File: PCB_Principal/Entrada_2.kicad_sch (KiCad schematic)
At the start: 17 parts, among them U41 TL071

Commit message: Iniciando PCB...
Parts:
- U151: renamed from U41; footprint Package_DIP:CERDIP-8_W7.62mm_SideBrazed_LongPads_Socket -> Package_DIP:CERDIP-8_W7.62mm_SideBrazed_LongPads
- renumbered C41 to C151, C42 to C152, C43 to C153, C44 to C154, C45 to C155, D41 to D151, D42 to D152, R41 to R151, R42 to R152, R43 to R153, R44 to R154, R45 to R155, R46 to R156, R47 to R157, R48 to R158, RV41 to RV151
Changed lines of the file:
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@@
 		(on_board yes)
 		(dnp no)
-		(property "Reference" "R44"
+		(property "Reference" "R154"
 			(at 185.42 91.948 90)
 			(effects
@@
 			(project "ISPEL-CAD_v1"
 				(path "/f66f0001-c0b9-4d2c-a26f-f2bac9dfd594/18a53c06-5390-4a02-a62f-2bcfe4b4c6e4"
-					(reference "R44")
+					(reference "R154")
 					(unit 1)
 				)
@@
 		(on_board yes)
 		(dnp no)
-		(property "Reference" "R42"
+		(property "Reference" "R152"
 			(at 104.14 89.408 90)
 			(effects
@@
 			(project "ISPEL-CAD_v1"
 				(path "/f66f0001-c0b9-4d2c-a26f-f2bac9dfd594/18a53c06-5390-4a02-a62f-2bcfe4b4c6e4"
-					(reference "R42")
+					(reference "R152")
 					(unit 1)
 				)
@@
 		(on_board yes)
 		(dnp no)
-		(property "Reference" "R47"
+		(property "Reference" "R157"
 			(at 209.55 86.36 0)
 			(effects
@@
 			(project "ISPEL-CAD_v1"
 				(path "/f66f0001-c0b9-4d2c-a26f-f2bac9dfd594/18a53c06-5390-4a02-a62f-2bcfe4b4c6e4"
-					(reference "R47")
+					(reference "R157")
 					(unit 1)
 				)
@@
 		(on_board yes)
 		(dnp no)
-		(property "Reference" "R46"
+		(property "Reference" "R156"
 			(at 201.93 91.948 90)
 			(effects
@@
 			(project "ISPEL-CAD_v1"
 				(path "/f66f0001-c0b9-4d2c-a26f-f2bac9dfd594/18a53c06-5390-4a02-a62f-2bcfe4b4c6e4"
-					(reference "R46")
+					(reference "R156")
 					(unit 1)
 				)
@@
 		(on_board yes)
 		(dnp no)
-		(property "Reference" "R43"
+		(property "Reference" "R153"
 			(at 111.76 99.06 0)
 			(effects
@@
 			(project "ISPEL-CAD_v1"
 				(path "/f66f0001-c0b9-4d2c-a26f-f2bac9dfd594/18a53c06-5390-4a02-a62f-2bcfe4b4c6e4"
-					(reference "R43")
+					(reference "R153")
 					(unit 1)
 				)
@@
 		(dnp no)
 		(fields_autoplaced yes)
-		(property "Reference" "C41"
+		(property "Reference" "C151"
 			(at 87.63 96.5262 0)
 			(effects
@@
 			(project "ISPEL-CAD_v1"
 				(path "/f66f0001-c0b9-4d2c-a26f-f2bac9dfd594/18a53c06-5390-4a02-a62f-2bcfe4b4c6e4"
-					(reference "C41")
+					(reference "C151")
 					(unit 1)
 				)
@@
 		(dnp no)
 		(fields_autoplaced yes)
-		(property "Reference" "#PWR047"
+		(property "Reference" "#PWR0157"
 			(at 222.25 90.17 0)
 			(effects
@@
 			(project "ISPEL-CAD_v1"
 				(path "/f66f0001-c0b9-4d2c-a26f-f2bac9dfd594/18a53c06-5390-4a02-a62f-2bcfe4b4c6e4"
-					(reference "#PWR047")
+					(reference "#PWR0157")
 					(unit 1)
 				)
@@
 		(on_board yes)
 		(dnp no)
-		(property "Reference" "C44"
+		(property "Reference" "C154"
 			(at 146.05 125.222 90)
 			(effects
@@
 			(project "ISPEL-CAD_v1"
 				(path "/f66f0001-c0b9-4d2c-a26f-f2bac9dfd594/18a53c06-5390-4a02-a62f-2bcfe4b4c6e4"
-					(reference "C44")
+					(reference "C154")
 					(unit 1)
 				)
@@
 		(dnp no)
 		(fields_autoplaced yes)
-		(property "Reference" "#PWR043"
+		(property "Reference" "#PWR0153"
 			(at 143.51 119.38 0)
 			(effects
@@
 			(project "ISPEL-CAD_v1"
 				(path "/f66f0001-c0b9-4d2c-a26f-f2bac9dfd594/18a53c06-5390-4a02-a62f-2bcfe4b4c6e4"
-					(reference "#PWR043")
+					(reference "#PWR0153")
 					(unit 1)
 				)
@@
 		(on_board yes)
 		(dnp no)
-		(property "Reference" "RV41"
+		(property "Reference" "RV151"
 			(at 143.51 106.68 90)
 			(effects
@@
 			(project "ISPEL-CAD_v1"
 				(path "/f66f0001-c0b9-4d2c-a26f-f2bac9dfd594/18a53c06-5390-4a02-a62f-2bcfe4b4c6e4"
-					(reference "RV41")
+					(reference "RV151")
 					(unit 1)
 				)
@@
 		(dnp no)
 		(fields_autoplaced yes)
-		(property "Reference" "C43"
+		(property "Reference" "C153"
 			(at 146.05 60.96 90)
 			(effects
@@
 			(project "ISPEL-CAD_v1"
 				(path "/f66f0001-c0b9-4d2c-a26f-f2bac9dfd594/18a53c06-5390-4a02-a62f-2bcfe4b4c6e4"
-					(reference "C43")
+					(reference "C153")
 					(unit 1)
 				)
@@
 		(dnp no)
 		(fields_autoplaced yes)
-		(property "Reference" "#PWR044"
+		(property "Reference" "#PWR0154"
 			(at 152.4 76.2 0)
 			(effects
@@
 			(project "ISPEL-CAD_v1"
 				(path "/f66f0001-c0b9-4d2c-a26f-f2bac9dfd594/18a53c06-5390-4a02-a62f-2bcfe4b4c6e4"
-					(reference "#PWR044")
+					(reference "#PWR0154")
 					(unit 1)
 				)
@@
 		(dnp no)
 		(fields_autoplaced yes)
-		(property "Reference" "D41"
+		(property "Reference" "D151"
 			(at 100.33 71.1199 90)
 			(effects
@@
 			(project "ISPEL-CAD_v1"
 				(path "/f66f0001-c0b9-4d2c-a26f-f2bac9dfd594/18a53c06-5390-4a02-a62f-2bcfe4b4c6e4"
-					(reference "D41")
+					(reference "D151")
 					(unit 1)
 				)
@@
 		(dnp no)
 		(fields_autoplaced yes)
-		(property "Reference" "C42"
+		(property "Reference" "C152"
 			(at 91.4463 78.74 90)
 			(effects
@@
 			(project "ISPEL-CAD_v1"
 				(path "/f66f0001-c0b9-4d2c-a26f-f2bac9dfd594/18a53c06-5390-4a02-a62f-2bcfe4b4c6e4"
-					(reference "C42")
+					(reference "C152")
 					(unit 1)
 				)
@@
 		(on_board yes)
 		(dnp no)
-		(property "Reference" "R48"
+		(property "Reference" "R158"
 			(at 209.55 100.33 0)
 			(effects
@@
 			(project "ISPEL-CAD_v1"
 				(path "/f66f0001-c0b9-4d2c-a26f-f2bac9dfd594/18a53c06-5390-4a02-a62f-2bcfe4b4c6e4"
-					(reference "R48")
+					(reference "R158")
 					(unit 1)
 				)
@@
 		(dnp no)
 		(fields_autoplaced yes)
-		(property "Reference" "#PWR041"
+		(property "Reference" "#PWR0151"
 			(at 85.09 110.49 0)
 			(effects
@@
 			(project "ISPEL-CAD_v1"
 				(path "/f66f0001-c0b9-4d2c-a26f-f2bac9dfd594/18a53c06-5390-4a02-a62f-2bcfe4b4c6e4"
-					(reference "#PWR041")
+					(reference "#PWR0151")
 					(unit 1)
 				)
@@
 		(dnp no)
 		(fields_autoplaced yes)
-		(property "Reference" "D42"
+		(property "Reference" "D152"
 			(at 100.33 109.2199 90)
 			(effects
@@
 			(project "ISPEL-CAD_v1"
 				(path "/f66f0001-c0b9-4d2c-a26f-f2bac9dfd594/18a53c06-5390-4a02-a62f-2bcfe4b4c6e4"
-					(reference "D42")
+					(reference "D152")
 					(unit 1)
 				)
@@
 		(on_board yes)
 		(dnp no)
-		(property "Reference" "U41"
+		(property "Reference" "U151"
 			(at 142.24 86.36 0)
 			(effects
@@
 			)
 		)
-		(property "Footprint" "Package_DIP:CERDIP-8_W7.62mm_SideBrazed_LongPads_Socket"
+		(property "Footprint" "Package_DIP:CERDIP-8_W7.62mm_SideBrazed_LongPads"
 			(at 140.97 92.71 0)
 			(effects
@@
 			(project "ISPEL-CAD_v1"
 				(path "/f66f0001-c0b9-4d2c-a26f-f2bac9dfd594/18a53c06-5390-4a02-a62f-2bcfe4b4c6e4"
-					(reference "U41")
+					(reference "U151")
 					(unit 1)
 				)
@@
 		(dnp no)
 		(fields_autoplaced yes)
-		(property "Reference" "#PWR045"
+		(property "Reference" "#PWR0155"
 			(at 152.4 127 0)
 			(effects
@@
 			(project "ISPEL-CAD_v1"
 				(path "/f66f0001-c0b9-4d2c-a26f-f2bac9dfd594/18a53c06-5390-4a02-a62f-2bcfe4b4c6e4"
-					(reference "#PWR045")
+					(reference "#PWR0155")
 					(unit 1)
 				)
@@
 		(on_board yes)
 		(dnp no)
-		(property "Reference" "R45"
+		(property "Reference" "R155"
 			(at 195.58 86.36 0)
 			(effects
@@
 			(project "ISPEL-CAD_v1"
 				(path "/f66f0001-c0b9-4d2c-a26f-f2bac9dfd594/18a53c06-5390-4a02-a62f-2bcfe4b4c6e4"
-					(reference "R45")
+					(reference "R155")
 					(unit 1)
 				)
@@
 		(dnp no)
 		(fields_autoplaced yes)
-		(property "Reference" "C45"
+		(property "Reference" "C155"
 			(at 217.17 73.66 90)
 			(effects
@@
 			(project "ISPEL-CAD_v1"
 				(path "/f66f0001-c0b9-4d2c-a26f-f2bac9dfd594/18a53c06-5390-4a02-a62f-2bcfe4b4c6e4"
-					(reference "C45")
+					(reference "C155")
 					(unit 1)
 				)
@@
 		(dnp no)
 		(fields_autoplaced yes)
-		(property "Reference" "#PWR042"
+		(property "Reference" "#PWR0152"
 			(at 110.49 110.49 0)
 			(effects
@@
 			(project "ISPEL-CAD_v1"
 				(path "/f66f0001-c0b9-4d2c-a26f-f2bac9dfd594/18a53c06-5390-4a02-a62f-2bcfe4b4c6e4"
-					(reference "#PWR042")
+					(reference "#PWR0152")
 					(unit 1)
 				)
@@
 		(dnp no)
 		(fields_autoplaced yes)
-		(property "Reference" "#PWR046"
+		(property "Reference" "#PWR0156"
 			(at 208.28 113.03 0)
 			(effects
@@
 			(project "ISPEL-CAD_v1"
 				(path "/f66f0001-c0b9-4d2c-a26f-f2bac9dfd594/18a53c06-5390-4a02-a62f-2bcfe4b4c6e4"
-					(reference "#PWR046")
+					(reference "#PWR0156")
 					(unit 1)
 				)
@@
 		(on_board yes)
 		(dnp no)
-		(property "Reference" "R41"
+		(property "Reference" "R151"
 			(at 91.44 89.408 90)
 			(effects
@@
 			(project "ISPEL-CAD_v1"
 				(path "/f66f0001-c0b9-4d2c-a26f-f2bac9dfd594/18a53c06-5390-4a02-a62f-2bcfe4b4c6e4"
-					(reference "R41")
-					(unit 1)
-				)
+					(reference "R151")
+					(unit 1)
+				)

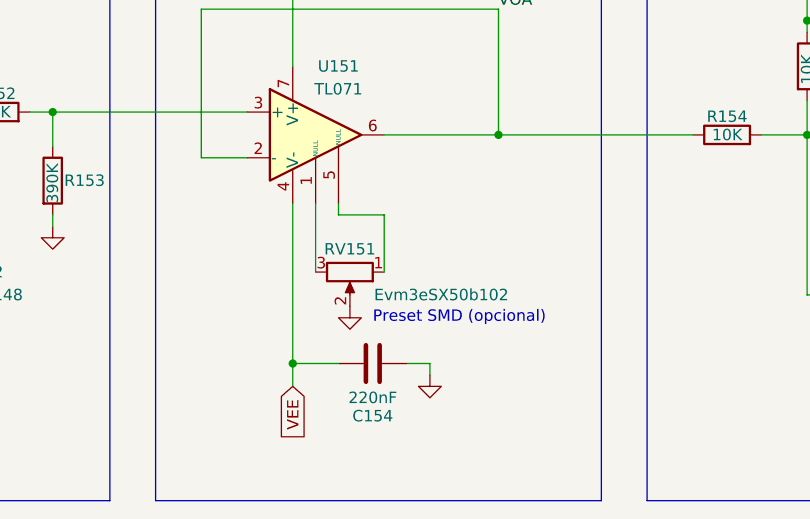
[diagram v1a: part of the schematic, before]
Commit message: Placa con conector J8.
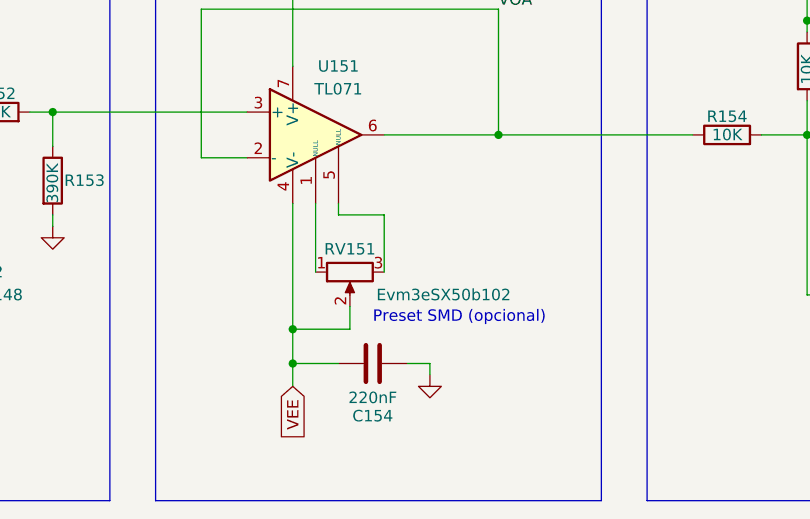
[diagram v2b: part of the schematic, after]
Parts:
- U151: footprint Package_DIP:CERDIP-8_W7.62mm_SideBrazed_LongPads -> Package_DIP:CERDIP-8_W7.62mm_SideBrazed_LongPads_Socket
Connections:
- net GND: no longer RV151.2
- net VEE: now also RV151.2
- net at RV151.1: now also U151.1 (NULL); no longer U151.5 (NULL)
- net at RV151.3: now also U151.5 (NULL); no longer U151.1 (NULL)
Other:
- moved on the sheet: RV151
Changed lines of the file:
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@@
+	)
+	(junction
+		(at 137.16 115.57)
+		(diameter 0)
+		(color 0 0 0 0)
 	)
 	(junction
@@
 	(wire
 		(pts
-			(xy 137.16 101.6) (xy 137.16 119.38)
+			(xy 143.51 113.03) (xy 143.51 115.57)
+		)
+		(stroke
+			(width 0)
+			(type default)
+		)
+	)
+	(wire
+		(pts
+			(xy 137.16 101.6) (xy 137.16 115.57)
 		)
 		(stroke
@@
 	(wire
 		(pts
+			(xy 137.16 115.57) (xy 143.51 115.57)
+		)
+		(stroke
+			(width 0)
+			(type default)
+		)
+	)
+	(wire
+		(pts
 			(xy 194.31 93.98) (xy 198.12 93.98)
 		)
@@
 		(pts
 			(xy 93.98 85.09) (xy 97.79 85.09)
+		)
+		(stroke
+			(width 0)
+			(type default)
+		)
+	)
+	(wire
+		(pts
+			(xy 137.16 115.57) (xy 137.16 119.38)
 		)
 		(stroke
@@
 	)
 	(symbol
-		(lib_id "power:GND")
-		(at 143.51 113.03 0)
-		(unit 1)
-		(exclude_from_sim no)
-		(in_bom yes)
-		(on_board yes)
-		(dnp no)
-		(fields_autoplaced yes)
-		(property "Reference" "#PWR0153"
-			(at 143.51 119.38 0)
-			(effects
-				(font
-					(size 1.27 1.27)
-				)
-				(hide yes)
-			)
-		)
-		(property "Value" "GND"
-			(at 143.51 118.11 0)
-			(effects
-				(font
-					(size 1.27 1.27)
-				)
-				(hide yes)
-			)
-		)
-		(property "Footprint" ""
-			(at 143.51 113.03 0)
-			(effects
-				(font
-					(size 1.27 1.27)
-				)
-				(hide yes)
-			)
-		)
-		(property "Datasheet" ""
-			(at 143.51 113.03 0)
-			(effects
-				(font
-					(size 1.27 1.27)
-				)
-				(hide yes)
-			)
-		)
-		(property "Description" "Power symbol creates a global label with name \"GND\" , ground"
-			(at 143.51 113.03 0)
-			(effects
-				(font
-					(size 1.27 1.27)
-				)
-				(hide yes)
-			)
-		)
-		(pin "1"
-		)
-		(instances
-			(project "ISPEL-CAD_v1"
-				(path "/f66f0001-c0b9-4d2c-a26f-f2bac9dfd594/18a53c06-5390-4a02-a62f-2bcfe4b4c6e4"
-					(reference "#PWR0153")
-					(unit 1)
-				)
-			)
-		)
-	)
-	(symbol
 		(lib_id "Device:R_Potentiometer")
-		(at 143.51 109.22 270)
+		(at 143.51 109.22 90)
+		(mirror x)
 		(unit 1)
 		(exclude_from_sim no)
@@
 		)
 		(property "Value" "Evm3eSX50b102"
-			(at 153.67 111.76 90)
+			(at 153.924 111.76 90)
 			(effects
 				(font
@@
 			)
 		)
-		(property "Footprint" "Package_DIP:CERDIP-8_W7.62mm_SideBrazed_LongPads"
+		(property "Footprint" "Package_DIP:CERDIP-8_W7.62mm_SideBrazed_LongPads_Socket"
 			(at 140.97 92.71 0)
 			(effects

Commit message: Revisión 1. Con prototipo ISPEL Beta 2024 en fase de prueba.
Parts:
- C152: value 3.3pF -> 5pF
- U151: value TL071 -> CA3140
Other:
- title: Entrada 2 (ISPEL Beta 2024) -> Entrada 2 (ISPEL Beta)
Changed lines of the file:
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@@
 	(paper "A4")
 	(title_block
-		(title "Entrada 2 (ISPEL Beta 2024)")
-		(rev "2 (GC)")
+		(title "Entrada 2 (ISPEL Beta)")
+		(date "2025-04-04")
+		(rev "1")
 		(company "UNDAV")
 	)
@@
 			)
 		)
-		(property "Value" "3.3pF"
+		(property "Value" "5pF"
 			(at 91.4463 81.28 90)
 			(effects
@@
 			)
 		)
-		(property "Value" "TL071"
+		(property "Value" "CA3140"
 			(at 142.24 88.9 0)
 			(effects
@@
 			)
 		)
-		(property "Datasheet" "http://www.ti.com/lit/ds/symlink/tl071.pdf"
+		(property "Datasheet" "https://www.renesas.com/en/document/dst/ca3140-ca3140a-datasheet?r=505296"
 			(at 143.51 90.17 0)
 			(effects
@@
 			)
 		)
-		(property "Description" "Single Low-Noise JFET-Input Operational Amplifiers, DIP-8/SOIC-8"
+		(property "Description" "4.5MHz, BiMOS Operational Amplifier with MOSFET Input/Bipolar Output"
 			(at 139.7 93.98 0)
 			(effects
